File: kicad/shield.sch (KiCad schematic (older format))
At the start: 35 parts, among them J1 Conn_01x11, J2 Conn_01x12, J3 Conn_01x24, Q1 ZXMN3B01F, Q39 Q_PNP_BEC, SW1 SW_Push, SW2 SW_Push, SW3 SW_Push, SW4 SW_Push

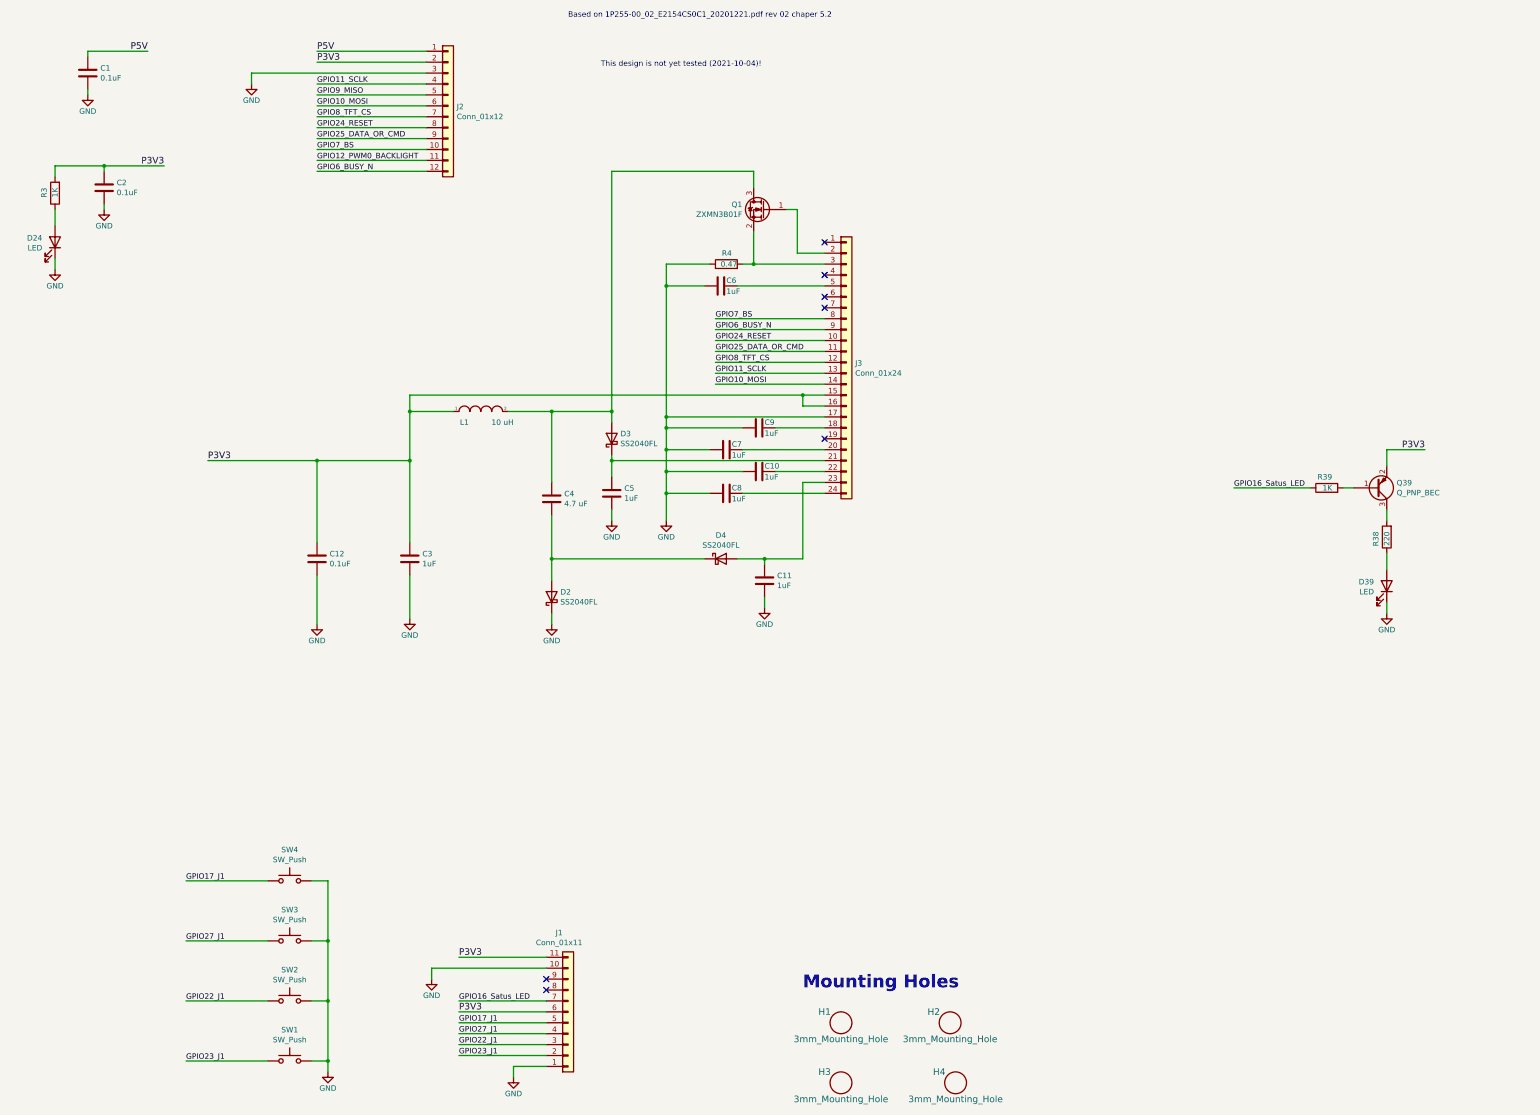
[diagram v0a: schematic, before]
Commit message: did routing, ready to be tested
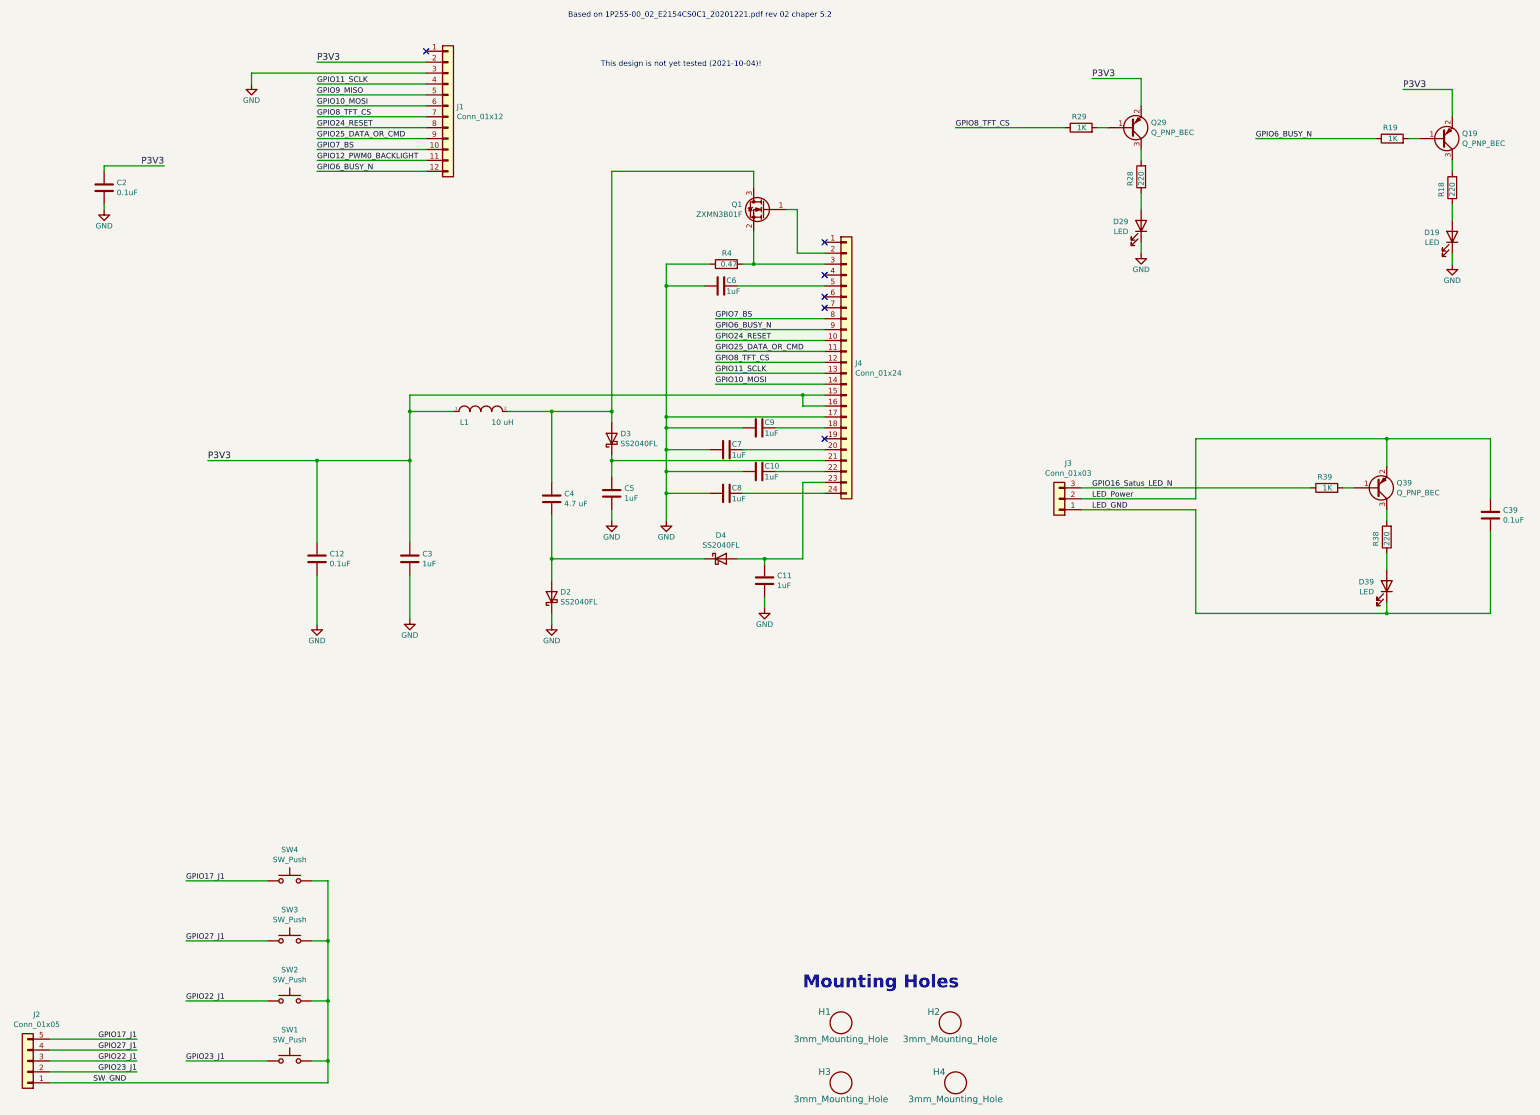
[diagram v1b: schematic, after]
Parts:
- removed D24: LED, LED_SMD:LED_0805_2012Metric, symbol Device:LED
- removed J1: Conn_01x11, Connector_PinHeader_2.54mm:PinHeader_1x11_P2.54mm_Vertical, symbol Connector_Generic:Conn_01x11
- removed R3: 1K, Resistor_SMD:R_0805_2012Metric_Pad1.15x1.40mm_HandSolder, symbol Device:R
- added D19, D29: LED, LED_THT:LED_D3.0mm, symbol Device:LED
- added J2: Conn_01x05, Connector_PinHeader_2.54mm:PinHeader_1x05_P2.54mm_Vertical, symbol Connector_Generic:Conn_01x05
- added J3: Conn_01x03, Connector_PinHeader_2.54mm:PinHeader_1x03_P2.54mm_Vertical, symbol Connector_Generic:Conn_01x03
- added Q19, Q29: Q_PNP_BEC, Package_TO_SOT_SMD:SOT-23, symbol Device:Q_PNP_BEC
- added R18, R28: 220, Resistor_SMD:R_0805_2012Metric_Pad1.15x1.40mm_HandSolder, symbol Device:R
- added R19, R29: 1K, Resistor_SMD:R_0805_2012Metric_Pad1.15x1.40mm_HandSolder, symbol Device:R
- D39: footprint LED_SMD:LED_0805_2012Metric -> LED_THT:LED_D3.0mm
- SW1, SW2, SW3, SW4: footprint Button_Switch_SMD:SW_SPST_TL3342 -> Button_Switch_THT:SW_TH_Tactile_Omron_B3F-10xx
- renumbered C1 to C39, J2 to J1, J3 to J4
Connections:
- net GND: now also D19.1 (K), D29.1 (K); no longer C39.2, D39.1 (K), SW1.2, SW2.2, SW3.2, SW4.2
- net GPIO17_J1: now also J2.5 (Pin_5)
- net GPIO22_J1: now also J2.3 (Pin_3)
- net GPIO23_J1: now also J2.2 (Pin_2)
- net GPIO27_J1: now also J2.4 (Pin_4)
- net GPIO6_BUSY_N: now also R19.1
- net GPIO8_TFT_CS: now also R29.1
- net P3V3: now also Q19.2 (E), Q29.2 (E); no longer Q39.2 (E)
- net GPIO16_Satus_LED renamed GPIO16_Satus_LED_N
- net GPIO16_Satus_LED_N: now also J3.3 (Pin_3)
- net P5V: no longer names the net of J1.1 (Pin_1)
- net P5V: no longer C39.1
- new net: Q29.1 (B), R29.2
- new net: Q29.3 (C), R28.2
- new net: D29.2 (A), R28.1
- new net: Q19.1 (B), R19.2
- new net: Q19.3 (C), R18.2
- new net: D19.2 (A), R18.1
- new net LED_GND: C39.2, D39.1 (K), J3.1 (Pin_1)
- new net LED_Power: C39.1, J3.2 (Pin_2), Q39.2 (E)
- new net SW_GND: J2.1 (Pin_1), SW1.2, SW2.2, SW3.2, SW4.2
- no-connect marks 7 -> 6
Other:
- moved on the sheet: C39

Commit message: added power LED
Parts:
- added D99: LED, LED_THT:LED_D3.0mm, symbol Device:LED
- added R98: 1K, Resistor_SMD:R_0805_2012Metric_Pad1.15x1.40mm_HandSolder, symbol Device:R
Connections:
- net GND: now also D99.1 (K)
- net P3V3: now also R98.2
- new net: D99.2 (A), R98.1
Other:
- note added: "Pin 1, reserved for 5 Volt"
- moved on the sheet: C39, D39, J3, Q39, R38, R39
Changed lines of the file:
@@
 Sheet 1 1
 Title "pervasive display shield"
-Date "2021-10-13"
+Date "2021-10-18"
 Rev "NOTE This is not tested!"
 Comp "Drekkar AB"
@@
 L Device:Q_PNP_BEC Q39
 U 1 1 60C8825C
-P 13000 5350
-F 0 "Q39" H 13190 5304 50  0000 L CNN
-F 1 "Q_PNP_BEC" H 13190 5395 50  0000 L CNN
-F 2 "Package_TO_SOT_SMD:SOT-23" H 13200 5450 50  0001 C CNN
-F 3 "~" H 13000 5350 50  0001 C CNN
-	1    13000 5350
+P 12350 7750
+F 0 "Q39" H 12540 7704 50  0000 L CNN
+F 1 "Q_PNP_BEC" H 12540 7795 50  0000 L CNN
+F 2 "Package_TO_SOT_SMD:SOT-23" H 12550 7850 50  0001 C CNN
+F 3 "~" H 12350 7750 50  0001 C CNN
+	1    12350 7750
 	1    0    0    1
 $EndComp
@@
 L Device:R R39
 U 1 1 60CE4AF0
-P 12550 5350
-F 0 "R39" V 12650 5300 50  0000 L CNN
-F 1 "1K" V 12550 5300 50  0000 L CNN
-F 2 "Resistor_SMD:R_0805_2012Metric_Pad1.15x1.40mm_HandSolder" V 12480 5350 50  0001 C CNN
-F 3 "~" H 12550 5350 50  0001 C CNN
-	1    12550 5350
+P 11900 7750
+F 0 "R39" V 12000 7700 50  0000 L CNN
+F 1 "1K" V 11900 7700 50  0000 L CNN
+F 2 "Resistor_SMD:R_0805_2012Metric_Pad1.15x1.40mm_HandSolder" V 11830 7750 50  0001 C CNN
+F 3 "~" H 11900 7750 50  0001 C CNN
+	1    11900 7750
 	0    -1   -1   0
 $EndComp
 Wire Wire Line
-	12700 5350 12800 5350
+	12050 7750 12150 7750
 $Comp
 L Device:LED D39
 U 1 1 60D01AC1
-P 13100 6250
-F 0 "D39" V 13139 6133 50  0000 R CNN
-F 1 "LED" V 13048 6133 50  0000 R CNN
-F 2 "LED_THT:LED_D3.0mm" H 13100 6250 50  0001 C CNN
-F 3 "~" H 13100 6250 50  0001 C CNN
-	1    13100 6250
+P 12450 8650
+F 0 "D39" V 12489 8533 50  0000 R CNN
+F 1 "LED" V 12398 8533 50  0000 R CNN
+F 2 "LED_THT:LED_D3.0mm" H 12450 8650 50  0001 C CNN
+F 3 "~" H 12450 8650 50  0001 C CNN
+	1    12450 8650
 	0    1    -1   0
 $EndComp
 Wire Wire Line
-	13100 6100 13100 5950
-Wire Wire Line
-	13100 6500 13100 6400
+	12450 8500 12450 8350
+Wire Wire Line
+	12450 8900 12450 8800
 $Comp
 L Device:R R38
 U 1 1 610F3592
-P 13100 5800
-F 0 "R38" V 13200 5750 50  0000 L CNN
-F 1 "220" V 13100 5750 50  0000 L CNN
-F 2 "Resistor_SMD:R_0805_2012Metric_Pad1.15x1.40mm_HandSolder" V 13030 5800 50  0001 C CNN
-F 3 "~" H 13100 5800 50  0001 C CNN
-	1    13100 5800
+P 12450 8200
+F 0 "R38" V 12550 8150 50  0000 L CNN
+F 1 "220" V 12450 8150 50  0000 L CNN
+F 2 "Resistor_SMD:R_0805_2012Metric_Pad1.15x1.40mm_HandSolder" V 12380 8200 50  0001 C CNN
+F 3 "~" H 12450 8200 50  0001 C CNN
+	1    12450 8200
 	-1   0    0    1
 $EndComp
 Wire Wire Line
-	13100 5650 13100 5550
+	12450 8050 12450 7950
 $Comp
 L Connector_Generic:Conn_01x12 J1
@@
 $EndComp
 Wire Wire Line
-	10300 5450 11350 5450
-Wire Wire Line
-	11350 5450 11350 4900
-Wire Wire Line
-	11350 4900 13100 4900
-Wire Wire Line
-	13100 4900 13100 5150
-Wire Wire Line
-	13100 6500 11350 6500
-Wire Wire Line
-	11350 5550 11350 6500
-Wire Wire Line
-	10300 5550 11350 5550
-Text Label 10400 5450 0    50   ~ 0
+	9650 7850 10700 7850
+Wire Wire Line
+	10700 7850 10700 7300
+Wire Wire Line
+	10700 7300 12450 7300
+Wire Wire Line
+	12450 7300 12450 7550
+Wire Wire Line
+	12450 8900 10700 8900
+Wire Wire Line
+	10700 7950 10700 8900
+Wire Wire Line
+	9650 7950 10700 7950
+Text Label 9750 7850 0    50   ~ 0
 LED_Power
-Text Label 10400 5550 0    50   ~ 0
+Text Label 9750 7950 0    50   ~ 0
 LED_GND
 Wire Wire Line
-	10300 5350 12400 5350
+	9650 7750 11750 7750
 $Comp
 L Device:C C39
 U 1 1 5F43CD9B
-P 14050 5600
-F 0 "C39" H 14165 5646 50  0000 L CNN
-F 1 "0.1uF" H 14165 5555 50  0000 L CNN
-F 2 "Capacitor_SMD:C_0805_2012Metric" H 14088 5450 50  0001 C CNN
-F 3 "~" H 14050 5600 50  0001 C CNN
-	1    14050 5600
-	1    0    0    -1
-$EndComp
-Wire Wire Line
-	14050 4900 13100 4900
-Wire Wire Line
-	14050 4900 14050 5450
-Connection ~ 13100 4900
-Wire Wire Line
-	14050 6500 13100 6500
-Wire Wire Line
-	14050 5750 14050 6500
-Connection ~ 13100 6500
+P 13400 8000
+F 0 "C39" H 13515 8046 50  0000 L CNN
+F 1 "0.1uF" H 13515 7955 50  0000 L CNN
+F 2 "Capacitor_SMD:C_0805_2012Metric" H 13438 7850 50  0001 C CNN
+F 3 "~" H 13400 8000 50  0001 C CNN
+	1    13400 8000
+	1    0    0    -1
+$EndComp
+Wire Wire Line
+	13400 7300 12450 7300
+Wire Wire Line
+	13400 7300 13400 7850
+Connection ~ 12450 7300
+Wire Wire Line
+	13400 8900 12450 8900
+Wire Wire Line
+	13400 8150 13400 8900
+Connection ~ 12450 8900
 Wire Wire Line
 	850  10800 3400 10800
 Wire Wire Line
 	3400 10600 3400 10800
-Text Label 10400 5350 0    50   ~ 0
+Text Label 9750 7750 0    50   ~ 0
 GPIO16_Satus_LED_N
 $Comp
@@
 L Connector_Generic:Conn_01x03 J3
 U 1 1 6180A6AD
-P 10100 5450
-F 0 "J3" H 10018 5125 50  0000 C CNN
-F 1 "Conn_01x03" H 10018 5216 50  0000 C CNN
-F 2 "Connector_PinHeader_2.54mm:PinHeader_1x03_P2.54mm_Vertical" H 10100 5450 50  0001 C CNN
-F 3 "~" H 10100 5450 50  0001 C CNN
-	1    10100 5450
+P 9450 7850
+F 0 "J3" H 9368 7525 50  0000 C CNN
+F 1 "Conn_01x03" H 9368 7616 50  0000 C CNN
+F 2 "Connector_PinHeader_2.54mm:PinHeader_1x03_P2.54mm_Vertical" H 9450 7850 50  0001 C CNN
+F 3 "~" H 9450 7850 50  0001 C CNN
+	1    9450 7850
 	-1   0    0    1
 $EndComp
@@
 	1    0    0    -1
 $EndComp
+$Comp
+L Device:LED D99
+U 1 1 616DC77B
+P 12200 5300
+F 0 "D99" V 12239 5183 50  0000 R CNN
+F 1 "LED" V 12148 5183 50  0000 R CNN
+F 2 "LED_THT:LED_D3.0mm" H 12200 5300 50  0001 C CNN
+F 3 "~" H 12200 5300 50  0001 C CNN
+	1    12200 5300
+	0    1    -1   0
+$EndComp
+Wire Wire Line
+	12200 5150 12200 5000
+Wire Wire Line
+	12200 5550 12200 5450
+$Comp
+L Device:R R98
+U 1 1 616DC787
+P 12200 4850
+F 0 "R98" V 12300 4800 50  0000 L CNN
+F 1 "1K" V 12200 4800 50  0000 L CNN
+F 2 "Resistor_SMD:R_0805_2012Metric_Pad1.15x1.40mm_HandSolder" V 12130 4850 50  0001 C CNN
+F 3 "~" H 12200 4850 50  0001 C CNN
+	1    12200 4850
+	-1   0    0    1
+$EndComp
+Wire Wire Line
+	12200 4700 12200 4600
+$Comp
+L power:GND #PWR0103
+U 1 1 616DC792
+P 12200 5550
+F 0 "#PWR0103" H 12200 5300 50  0001 C CNN
+F 1 "GND" H 12200 5400 50  0000 C CNN
+F 2 "" H 12200 5550 50  0000 C CNN
+F 3 "" H 12200 5550 50  0000 C CNN
+	1    12200 5550
+	-1   0    0    -1
+$EndComp
+Wire Wire Line
+	11200 4600 12200 4600
+Text Label 11200 4600 0    60   ~ 0
+P3V3
+Text Notes 3300 1350 0    50   ~ 0
+Pin 1, reserved for 5 Volt
 $EndSCHEMATC
